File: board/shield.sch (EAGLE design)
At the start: 44 parts, among them IC1 LM75, J1 WEALTHMETAL DS-214B, J2 22-05-7028-02, J3 22-05-7038-03, K1 G5L, T1 BC817, U1 LM2596S-5.0

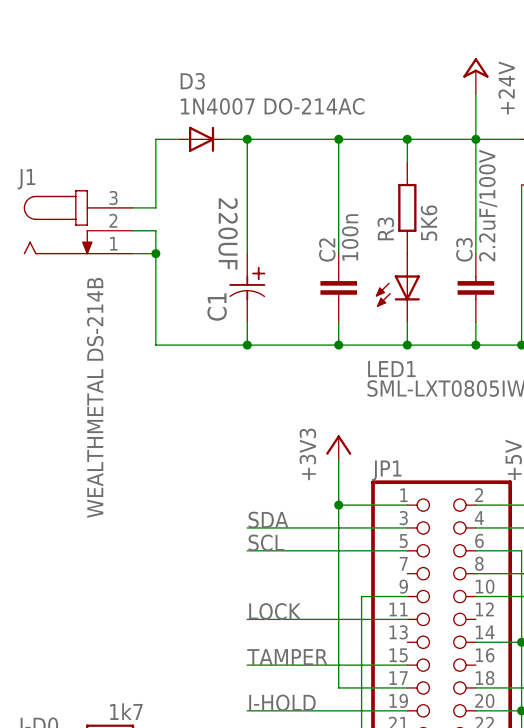
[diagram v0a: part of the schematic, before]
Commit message: DC Jack connector replaced
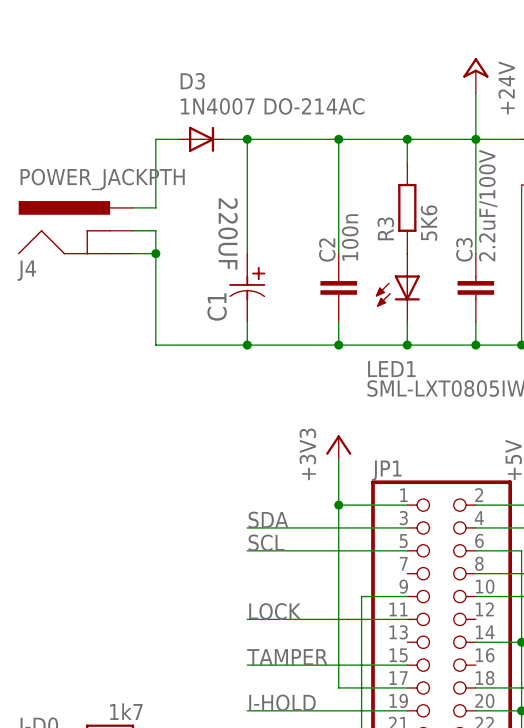
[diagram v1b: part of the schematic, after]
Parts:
- removed J1: WEALTHMETAL DS-214B, con-jack:JACK-PLUG0
- added J4: POWER_JACKPTH, SparkFun-Connectors:POWER_JACKPTH
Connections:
- net GND: now also J4.GND, J4.GNDBREAK; no longer J1.1, J1.2
- net UIN: now also J4.PWR; no longer J1.3
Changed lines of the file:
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@@
 <?xml version="1.0" encoding="utf-8"?>
 <!DOCTYPE eagle SYSTEM "eagle.dtd">
-<eagle version="7.5.0">
+<eagle version="7.7.0">
 <drawing>
 <settings>
@@
 <layer number="53" name="tPadExt" color="7" fill="1" visible="no" active="no"/>
 <layer number="54" name="bPadExt" color="1" fill="1" visible="no" active="no"/>
+<layer number="56" name="wert" color="7" fill="1" visible="no" active="no"/>
+<layer number="57" name="tCAD" color="7" fill="1" visible="no" active="no"/>
+<layer number="59" name="tCarbon" color="7" fill="1" visible="no" active="no"/>
+<layer number="60" name="bCarbon" color="7" fill="1" visible="no" active="no"/>
 <layer number="90" name="Modules" color="5" fill="1" visible="yes" active="yes"/>
 <layer number="91" name="Nets" color="2" fill="1" visible="yes" active="yes"/>
@@
 <layer number="99" name="SpiceOrder" color="5" fill="1" visible="yes" active="yes"/>
 <layer number="100" name="Muster" color="7" fill="1" visible="no" active="no"/>
+<layer number="101" name="Patch_Top" color="12" fill="4" visible="yes" active="yes"/>
+<layer number="102" name="Vscore" color="7" fill="1" visible="yes" active="yes"/>
+<layer number="103" name="tMap" color="7" fill="1" visible="yes" active="yes"/>
+<layer number="104" name="Name" color="16" fill="1" visible="yes" active="yes"/>
+<layer number="105" name="tPlate" color="7" fill="1" visible="yes" active="yes"/>
+<layer number="106" name="bPlate" color="7" fill="1" visible="yes" active="yes"/>
+<layer number="107" name="Crop" color="7" fill="1" visible="yes" active="yes"/>
+<layer number="108" name="tplace-old" color="10" fill="1" visible="yes" active="yes"/>
+<layer number="109" name="ref-old" color="11" fill="1" visible="yes" active="yes"/>
+<layer number="110" name="fp0" color="7" fill="1" visible="yes" active="yes"/>
+<layer number="111" name="LPC17xx" color="7" fill="1" visible="yes" active="yes"/>
+<layer number="112" name="tSilk" color="7" fill="1" visible="yes" active="yes"/>
+<layer number="113" name="IDFDebug" color="4" fill="1" visible="yes" active="yes"/>
+<layer number="114" name="Badge_Outline" color="7" fill="1" visible="yes" active="yes"/>
+<layer number="115" name="ReferenceISLANDS" color="7" fill="1" visible="yes" active="yes"/>
+<layer number="116" name="Patch_BOT" color="9" fill="4" visible="yes" active="yes"/>
+<layer number="118" name="Rect_Pads" color="7" fill="1" visible="yes" active="yes"/>
+<layer number="121" name="_tsilk" color="7" fill="1" visible="yes" active="yes"/>
+<layer number="122" name="_bsilk" color="7" fill="1" visible="yes" active="yes"/>
+<layer number="123" name="tTestmark" color="7" fill="1" visible="yes" active="yes"/>
+<layer number="124" name="bTestmark" color="7" fill="1" visible="yes" active="yes"/>
+<layer number="125" name="_tNames" color="7" fill="1" visible="yes" active="yes"/>
+<layer number="126" name="_bNames" color="7" fill="1" visible="yes" active="yes"/>
+<layer number="127" name="_tValues" color="7" fill="1" visible="yes" active="yes"/>
+<layer number="128" name="_bValues" color="7" fill="1" visible="yes" active="yes"/>
+<layer number="129" name="Mask" color="7" fill="1" visible="yes" active="yes"/>
+<layer number="131" name="tAdjust" color="7" fill="1" visible="yes" active="yes"/>
+<layer number="132" name="bAdjust" color="7" fill="1" visible="yes" active="yes"/>
+<layer number="144" name="Drill_legend" color="7" fill="1" visible="yes" active="yes"/>
+<layer number="150" name="Notes" color="7" fill="1" visible="yes" active="yes"/>
+<layer number="151" name="HeatSink" color="7" fill="1" visible="yes" active="yes"/>
+<layer number="152" name="_bDocu" color="7" fill="1" visible="yes" active="yes"/>
+<layer number="153" name="FabDoc1" color="7" fill="1" visible="yes" active="yes"/>
+<layer number="154" name="FabDoc2" color="7" fill="1" visible="yes" active="yes"/>
+<layer number="155" name="FabDoc3" color="7" fill="1" visible="yes" active="yes"/>
+<layer number="199" name="Contour" color="7" fill="1" visible="yes" active="yes"/>
+<layer number="200" name="200bmp" color="1" fill="10" visible="yes" active="yes"/>
+<layer number="201" name="201bmp" color="2" fill="10" visible="yes" active="yes"/>
+<layer number="202" name="202bmp" color="3" fill="10" visible="yes" active="yes"/>
+<layer number="203" name="203bmp" color="4" fill="10" visible="yes" active="yes"/>
+<layer number="204" name="204bmp" color="5" fill="10" visible="yes" active="yes"/>
+<layer number="205" name="205bmp" color="6" fill="10" visible="yes" active="yes"/>
+<layer number="206" name="206bmp" color="7" fill="10" visible="yes" active="yes"/>
+<layer number="207" name="207bmp" color="8" fill="10" visible="yes" active="yes"/>
+<layer number="208" name="208bmp" color="9" fill="10" visible="yes" active="yes"/>
+<layer number="209" name="209bmp" color="7" fill="1" visible="yes" active="yes"/>
+<layer number="210" name="210bmp" color="7" fill="1" visible="yes" active="yes"/>
+<layer number="211" name="211bmp" color="7" fill="1" visible="yes" active="yes"/>
+<layer number="212" name="212bmp" color="7" fill="1" visible="yes" active="yes"/>
+<layer number="213" name="213bmp" color="7" fill="1" visible="yes" active="yes"/>
+<layer number="214" name="214bmp" color="7" fill="1" visible="yes" active="yes"/>
+<layer number="215" name="215bmp" color="7" fill="1" visible="yes" active="yes"/>
+<layer number="216" name="216bmp" color="7" fill="1" visible="yes" active="yes"/>
+<layer number="217" name="217bmp" color="18" fill="1" visible="no" active="no"/>
+<layer number="218" name="218bmp" color="19" fill="1" visible="no" active="no"/>
+<layer number="219" name="219bmp" color="20" fill="1" visible="no" active="no"/>
+<layer number="220" name="220bmp" color="21" fill="1" visible="no" active="no"/>
+<layer number="221" name="221bmp" color="22" fill="1" visible="no" active="no"/>
+<layer number="222" name="222bmp" color="23" fill="1" visible="no" active="no"/>
+<layer number="223" name="223bmp" color="24" fill="1" visible="no" active="no"/>
+<layer number="224" name="224bmp" color="25" fill="1" visible="no" active="no"/>
+<layer number="225" name="225bmp" color="7" fill="1" visible="yes" active="yes"/>
+<layer number="226" name="226bmp" color="7" fill="1" visible="yes" active="yes"/>
+<layer number="227" name="227bmp" color="7" fill="1" visible="yes" active="yes"/>
+<layer number="228" name="228bmp" color="7" fill="1" visible="yes" active="yes"/>
+<layer number="229" name="229bmp" color="7" fill="1" visible="yes" active="yes"/>
+<layer number="230" name="230bmp" color="7" fill="1" visible="yes" active="yes"/>
+<layer number="231" name="231bmp" color="7" fill="1" visible="yes" active="yes"/>
+<layer number="248" name="Housing" color="7" fill="1" visible="yes" active="yes"/>
+<layer number="249" name="Edge" color="7" fill="1" visible="yes" active="yes"/>
 <layer number="250" name="Descript" color="3" fill="1" visible="yes" active="yes"/>
 <layer number="251" name="SMDround" color="12" fill="11" visible="no" active="no"/>
+<layer number="254" name="cooling" color="7" fill="1" visible="yes" active="yes"/>
+<layer number="255" name="routoute" color="7" fill="1" visible="yes" active="yes"/>
 </layers>
 <schematic xreflabel="%F%N/%S.%C%R" xrefpart="/%S.%C%R">
@@
 <part name="F1" library="ptc-littlefuse" deviceset="1812L" device="" value="PPTC1812SMD110/16V"/>
 <part name="PCB1" library="e14_Rpi3_RevA" deviceset="RPI3" device=""/>
-<part name="J1" library="con-jack" deviceset="JACK-PLUG" device="0" value="WEALTHMETAL DS-214B"/>
 <part name="P+6" library="supply1" deviceset="+5V" device=""/>
 <part name="J2" library="con-molex" deviceset="22-?-02" device="05-7028"/>
@@
 <part name="LED3" library="led" deviceset="LED" device="CHIPLED_0805" value="SML-LX0805SUGC-TR"/>
 <part name="C6" library="rcl" deviceset="C-EU" device="C0805" value="100n"/>
+<part name="J4" library="SparkFun-Connectors" deviceset="POWER_JACK" device="PTH"/>
 </parts>
 <sheets>
@@
 <instance part="F1" gate="G$1" x="175.26" y="142.24"/>
 <instance part="PCB1" gate="G$1" x="320.04" y="33.02"/>
-<instance part="J1" gate="G$1" x="53.34" y="132.08" smashed="yes">
-<attribute name="NAME" x="45.72" y="137.16" size="1.778" layer="95"/>
-<attribute name="VALUE" x="53.34" y="127" size="1.778" layer="96" rot="R270"/>
-</instance>
 <instance part="P+6" gate="1" x="233.68" y="106.68" rot="MR0"/>
 <instance part="J2" gate="-1" x="180.34" y="10.16"/>
@@
 <attribute name="VALUE" x="243.459" y="136.144" size="1.778" layer="96" rot="R90"/>
 </instance>
+<instance part="J4" gate="G$1" x="55.88" y="127"/>
 </instances>
 <busses>
@@
 <wire x1="101.6" y1="137.16" x2="101.6" y2="119.38" width="0.1524" layer="91"/>
 <junction x="101.6" y="119.38"/>
-<pinref part="J1" gate="G$1" pin="2"/>
 <wire x1="58.42" y1="132.08" x2="60.96" y2="132.08" width="0.1524" layer="91"/>
-<pinref part="J1" gate="G$1" pin="1"/>
 <wire x1="58.42" y1="129.54" x2="60.96" y2="129.54" width="0.1524" layer="91"/>
 <wire x1="60.96" y1="129.54" x2="60.96" y2="132.08" width="0.1524" layer="91"/>
@@
 <wire x1="96.52" y1="121.92" x2="96.52" y2="119.38" width="0.1524" layer="91"/>
 <junction x="96.52" y="119.38"/>
+<pinref part="J4" gate="G$1" pin="GNDBREAK"/>
+<pinref part="J4" gate="G$1" pin="GND"/>
 </segment>
 <segment>
@@
 <net name="UIN" class="0">
 <segment>
-<pinref part="J1" gate="G$1" pin="3"/>
 <wire x1="58.42" y1="134.62" x2="60.96" y2="134.62" width="0.1524" layer="91"/>
 <wire x1="60.96" y1="134.62" x2="60.96" y2="142.24" width="0.1524" layer="91"/>
 <wire x1="60.96" y1="142.24" x2="63.5" y2="142.24" width="0.1524" layer="91"/>
 <pinref part="D3" gate="G$1" pin="A"/>
-</segment>
-</net>
+<pinref part="J4" gate="G$1" pin="PWR"/>
+</segment>
+</net>

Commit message: Relay connector extended with common pin, connection to +24V is optional by solder bridge
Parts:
- removed J3: 22-05-7038-03, con-molex:22-05-7038-03
- added J1: 22-05-7048-04, con-molex:22-05-7048-04
- added SJ1: (no value), jumper:SJ
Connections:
- net N$10 renamed LOCK_T1_R
- net N$11 renamed LED
- net N$8 renamed RELAY_SW
- removed net N$5: J3-3.S, K12.S
- removed net N$7: J3-1.S, K12.O
- new net C: J1-1.S, K12.P, SJ1.1
- new net NC: J1-2.S, K12.O
- new net NO: J1-4.S, K12.S
- net +24V: now also SJ1.2; no longer K12.P
- net GND: now also J1-3.S; no longer J3-2.S
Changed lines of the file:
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@@
 <part name="P+6" library="supply1" deviceset="+5V" device=""/>
 <part name="J2" library="con-molex" deviceset="22-?-02" device="05-7028"/>
-<part name="J3" library="con-molex" deviceset="22-?-03" device="05-7038"/>
 <part name="P+7" library="supply1" deviceset="+24V" device=""/>
 <part name="SV1" library="con-lstb" deviceset="MA05-2" device="" value="S2G10"/>
@@
 <part name="C6" library="rcl" deviceset="C-EU" device="C0805" value="100n"/>
 <part name="J4" library="SparkFun-Connectors" deviceset="POWER_JACK" device="PTH"/>
+<part name="J1" library="con-molex" deviceset="22-?-04" device="05-7048"/>
+<part name="SJ1" library="jumper" deviceset="SJ" device=""/>
 </parts>
 <sheets>
@@
 <instance part="J2" gate="-1" x="180.34" y="10.16"/>
 <instance part="J2" gate="-2" x="180.34" y="7.62"/>
-<instance part="J3" gate="-1" x="261.62" y="88.9"/>
-<instance part="J3" gate="-2" x="261.62" y="86.36"/>
-<instance part="J3" gate="-3" x="261.62" y="83.82"/>
-<instance part="P+7" gate="1" x="251.46" y="101.6" rot="MR0"/>
+<instance part="P+7" gate="1" x="251.46" y="116.84" rot="MR0"/>
 <instance part="SV1" gate="G$1" x="81.28" y="7.62" rot="R180"/>
 <instance part="SV2" gate="G$1" x="116.84" y="7.62" rot="R180"/>
@@
 </instance>
 <instance part="J4" gate="G$1" x="55.88" y="127"/>
+<instance part="J1" gate="-1" x="261.62" y="91.44"/>
+<instance part="J1" gate="-2" x="261.62" y="88.9"/>
+<instance part="J1" gate="-3" x="261.62" y="86.36"/>
+<instance part="J1" gate="-4" x="261.62" y="83.82"/>
+<instance part="SJ1" gate="1" x="251.46" y="106.68" rot="R90"/>
 </instances>
 <busses>
@@
 <wire x1="251.46" y1="86.36" x2="251.46" y2="81.28" width="0.1524" layer="91"/>
 <pinref part="GND14" gate="1" pin="GND"/>
-<pinref part="J3" gate="-2" pin="S"/>
+<pinref part="J1" gate="-3" pin="S"/>
 </segment>
 <segment>
@@
 <segment>
 <pinref part="P+7" gate="1" pin="+24V"/>
-<pinref part="K1" gate="2" pin="P"/>
-<wire x1="251.46" y1="99.06" x2="251.46" y2="96.52" width="0.1524" layer="91"/>
+<wire x1="251.46" y1="114.3" x2="251.46" y2="111.76" width="0.1524" layer="91"/>
+<pinref part="SJ1" gate="1" pin="2"/>
 </segment>
 <segment>
@@
 </segment>
 </net>
-<net name="N$5" class="0">
+<net name="NO" class="0">
 <segment>
 <wire x1="246.38" y1="83.82" x2="259.08" y2="83.82" width="0.1524" layer="91"/>
-<pinref part="J3" gate="-3" pin="S"/>
 <pinref part="K1" gate="2" pin="S"/>
 <wire x1="246.38" y1="83.82" x2="246.38" y2="88.9" width="0.1524" layer="91"/>
-</segment>
-</net>
-<net name="N$8" class="0">
+<pinref part="J1" gate="-4" pin="S"/>
+</segment>
+</net>
+<net name="RELAY_SW" class="0">
 <segment>
 <pinref part="T1" gate="G$1" pin="C"/>
@@
 </segment>
 </net>
-<net name="N$10" class="0">
+<net name="LOCK_T1_R" class="0">
 <segment>
 <pinref part="T1" gate="G$1" pin="B"/>
@@
 </segment>
 </net>
-<net name="N$7" class="0">
-<segment>
-<pinref part="J3" gate="-1" pin="S"/>
+<net name="NC" class="0">
+<segment>
 <pinref part="K1" gate="2" pin="O"/>
 <wire x1="259.08" y1="88.9" x2="256.54" y2="88.9" width="0.1524" layer="91"/>
+<pinref part="J1" gate="-2" pin="S"/>
 </segment>
 </net>
@@
 </segment>
 </net>
-<net name="N$11" class="0">
+<net name="LED" class="0">
 <segment>
 <pinref part="R12" gate="G$1" pin="2"/>
@@
 </segment>
 </net>
+<net name="C" class="0">
+<segment>
+<pinref part="K1" gate="2" pin="P"/>
+<pinref part="J1" gate="-1" pin="S"/>
+<wire x1="251.46" y1="101.6" x2="251.46" y2="99.06" width="0.1524" layer="91"/>
+<wire x1="251.46" y1="99.06" x2="251.46" y2="96.52" width="0.1524" layer="91"/>
+<wire x1="259.08" y1="91.44" x2="259.08" y2="99.06" width="0.1524" layer="91"/>
+<wire x1="259.08" y1="99.06" x2="251.46" y2="99.06" width="0.1524" layer="91"/>
+<junction x="251.46" y="99.06"/>
+<pinref part="SJ1" gate="1" pin="1"/>
+</segment>
+</net>

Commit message: Silkscreen corrected
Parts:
- removed PCB1: RPI3, e14_Rpi3_RevA:RPI3
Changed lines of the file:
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@@
 <part name="D7" library="diode" deviceset="DIODE-" device="DO-214AC" value="1N4007 DO-214AC"/>
 <part name="F1" library="ptc-littlefuse" deviceset="1812L" device="" value="PPTC1812SMD110/16V"/>
-<part name="PCB1" library="e14_Rpi3_RevA" deviceset="RPI3" device=""/>
 <part name="P+6" library="supply1" deviceset="+5V" device=""/>
 <part name="J2" library="con-molex" deviceset="22-?-02" device="05-7028"/>
@@
 </instance>
 <instance part="F1" gate="G$1" x="175.26" y="142.24"/>
-<instance part="PCB1" gate="G$1" x="320.04" y="33.02"/>
 <instance part="P+6" gate="1" x="233.68" y="106.68" rot="MR0"/>
 <instance part="J2" gate="-1" x="180.34" y="10.16"/>
@@
 </schematic>
 </drawing>
-<compatibility>
-<note version="6.3" minversion="6.2.2" severity="warning">
-Since Version 6.2.2 text objects can contain more than one line,
-which will not be processed correctly with this version.
-</note>
-</compatibility>
 </eagle>
